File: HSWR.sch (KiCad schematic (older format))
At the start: 25 parts, among them J1 USB_B, J2 IO, J3 B+, J4 B-, J5 U, J6 V, J7 W

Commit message: - reworked IO section -> now fully isolated - added fan output - sensor IO is now differential - exposed differential UART interface - fan pin not defined yet!
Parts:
- removed J2: IO, Auktora:PinHeader_2x10_P2.54mm_Vertical, symbol HSWR:Conn_01x20_Male_56
- removed JP1: 5V/3V3, Jumper:SolderJumper-3_P1.3mm_Open_RoundedPad1.0x1.5mm, symbol Jumper:Jumper_3_Open
- removed JP2, JP3: opt., Jumper:SolderJumper-2_P1.3mm_Open_RoundedPad1.0x1.5mm, symbol Device:Jumper_NO_Small
- removed R1, R2: 1k, Resistor_SMD:R_0805_2012Metric, symbol Device:R
- removed R3, R4: 1k5, Resistor_SMD:R_0805_2012Metric, symbol Device:R
- added J2: IO, Connector_IDC:IDC-Header_2x08_P2.54mm_Vertical_Lock, symbol Connector:Conn_01x16_Male
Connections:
- net labels removed: +5V
- wire segments 87 -> 70

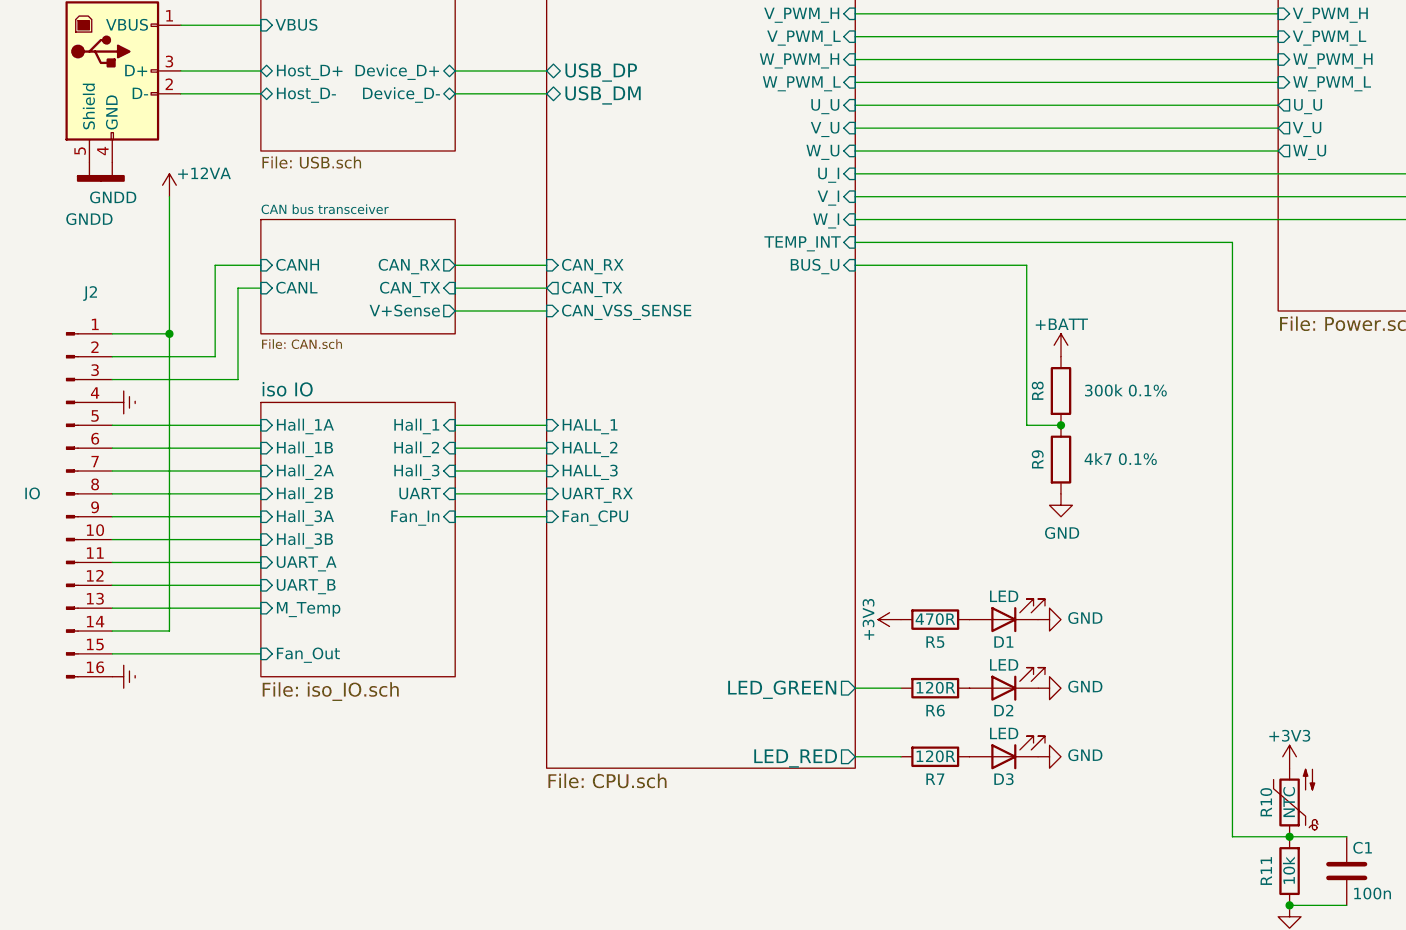
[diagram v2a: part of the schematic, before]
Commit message: - enlarged isolated island - bigger package for fan MOSFET - added 12V input protection - added U_DC sensing filter - added M_temp input filter - added reset pin decoupling for AVR - added HALL pull-ups - added TRI state selector jumper for buffer - removed UART selector jumper (AVR will check and switch to TRI state if needed)
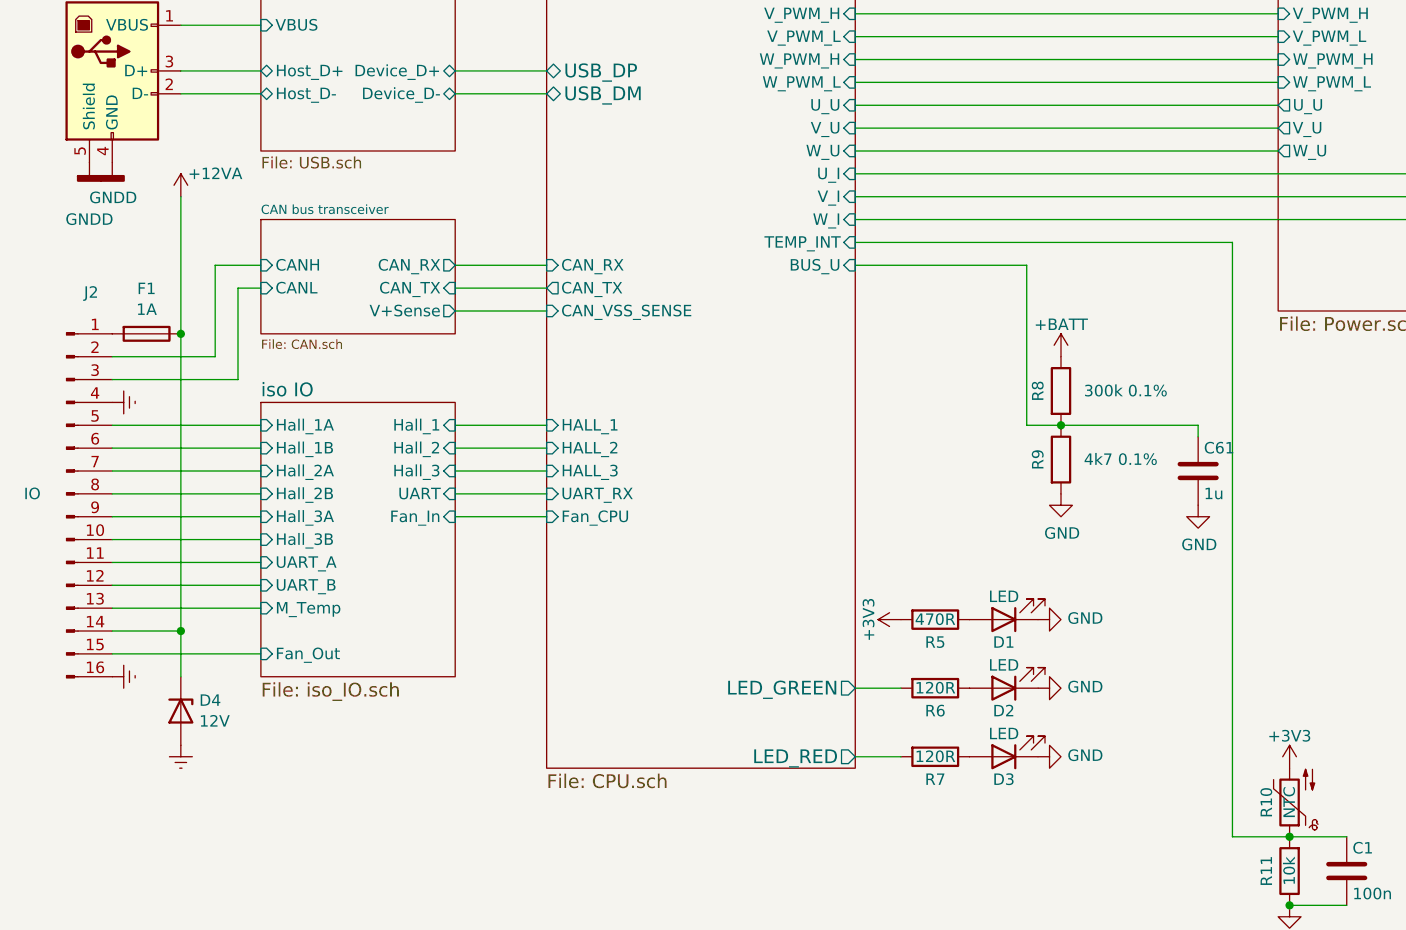
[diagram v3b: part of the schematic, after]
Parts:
- added C61: 1u, Capacitor_SMD:C_0805_2012Metric, symbol Device:C
- added D4: 12V, Diode_SMD:D_SMA, symbol Device:D_Zener
- added F1: 1A, Fuse:Fuse_Littelfuse-NANO2-451_453, symbol Device:Fuse
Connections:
- net +12VA: now also D4.1 (K), F1.1; no longer J2.1 (Pin_1)
- net Earth: now also D4.2 (A)
- net GND: now also C61.2
- net MCU/BUS_U: now also C61.1
- new net: F1.2, J2.1 (Pin_1)
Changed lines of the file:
@@
 EESchema Schematic File Version 4
+LIBS:HSWR-cache
 EELAYER 30 0
 EELAYER END
@@
 L power:+12VA #PWR03
 U 1 1 5C9EFA56
-P 1300 3500
-F 0 "#PWR03" H 1300 3350 50  0001 C CNN
-F 1 "+12VA" H 1450 3600 50  0000 C CNN
-F 2 "" H 1300 3500 50  0001 C CNN
-F 3 "" H 1300 3500 50  0001 C CNN
-	1    1300 3500
+P 1350 3500
+F 0 "#PWR03" H 1350 3350 50  0001 C CNN
+F 1 "+12VA" H 1500 3600 50  0000 C CNN
+F 2 "" H 1350 3500 50  0001 C CNN
+F 3 "" H 1350 3500 50  0001 C CNN
+	1    1350 3500
 	1    0    0    -1
 $EndComp
@@
 Connection ~ 6200 6600
 Wire Wire Line
-	1300 3500 1300 4100
-Wire Wire Line
-	1300 4100 1050 4100
-Wire Wire Line
 	1050 4200 1500 4200
 Wire Wire Line
@@
 	1700 5300 1050 5300
 Wire Wire Line
-	1300 4100 1300 5400
-Wire Wire Line
-	1300 5400 1050 5400
-Connection ~ 1300 4100
+	1350 5400 1050 5400
 $Comp
 L power:Earth #PWR0119
@@
 	1    0    0    -1
 $EndComp
+$Comp
+L Device:C C61
+U 1 1 5E6496A9
+P 5800 4700
+F 0 "C61" H 5825 4800 50  0000 L CNN
+F 1 "1u" H 5825 4600 50  0000 L CNN
+F 2 "Capacitor_SMD:C_0805_2012Metric" H 5838 4550 50  0001 C CNN
+F 3 "" H 5800 4700 50  0000 C CNN
+	1    5800 4700
+	1    0    0    -1
+$EndComp
+$Comp
+L power:GND #PWR0152
+U 1 1 5E64A18C
+P 5800 4850
+F 0 "#PWR0152" H 5800 4600 50  0001 C CNN
+F 1 "GND" H 5805 4677 50  0000 C CNN
+F 2 "" H 5800 4850 50  0001 C CNN
+F 3 "" H 5800 4850 50  0001 C CNN
+	1    5800 4850
+	1    0    0    -1
+$EndComp
+Wire Wire Line
+	5800 4550 5800 4500
+Wire Wire Line
+	5800 4500 5200 4500
+Wire Wire Line
+	1350 3500 1350 4100
+$Comp
+L Device:Fuse F1
+U 1 1 5E72429D
+P 1200 4100
+F 0 "F1" V 1003 4100 50  0000 C CNN
+F 1 "1A" V 1094 4100 50  0000 C CNN
+F 2 "Fuse:Fuse_Littelfuse-NANO2-451_453" V 1130 4100 50  0001 C CNN
+F 3 "~" H 1200 4100 50  0001 C CNN
+	1    1200 4100
+	0    1    1    0
+$EndComp
+Connection ~ 1350 4100
+Wire Wire Line
+	1350 4100 1350 5400
+$Comp
+L Device:D_Zener D4
+U 1 1 5E727A0D
+P 1350 5750
+F 0 "D4" V 1304 5830 50  0000 L CNN
+F 1 "12V" V 1395 5830 50  0000 L CNN
+F 2 "Diode_SMD:D_SMA" H 1350 5750 50  0001 C CNN
+F 3 "~" H 1350 5750 50  0001 C CNN
+	1    1350 5750
+	0    1    1    0
+$EndComp
+Wire Wire Line
+	1350 5400 1350 5600
+Connection ~ 1350 5400
+$Comp
+L power:Earth #PWR0155
+U 1 1 5E72D56C
+P 1350 5900
+F 0 "#PWR0155" H 1350 5650 50  0001 C CNN
+F 1 "Earth" H 1350 5750 50  0001 C CNN
+F 2 "" H 1350 5900 60  0000 C CNN
+F 3 "" H 1350 5900 60  0000 C CNN
+	1    1350 5900
+	1    0    0    -1
+$EndComp

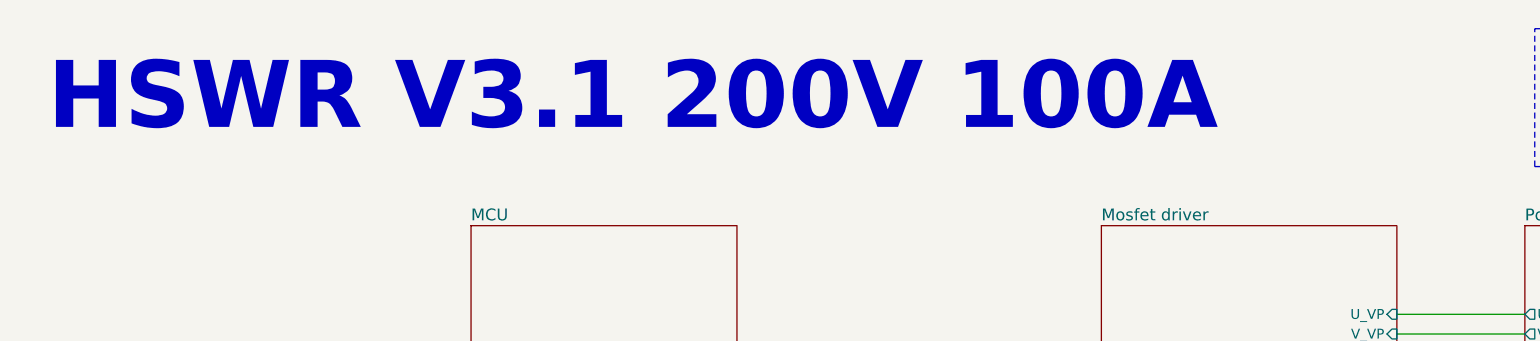
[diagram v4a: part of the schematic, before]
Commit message: - updated schematic textbox (version, author)
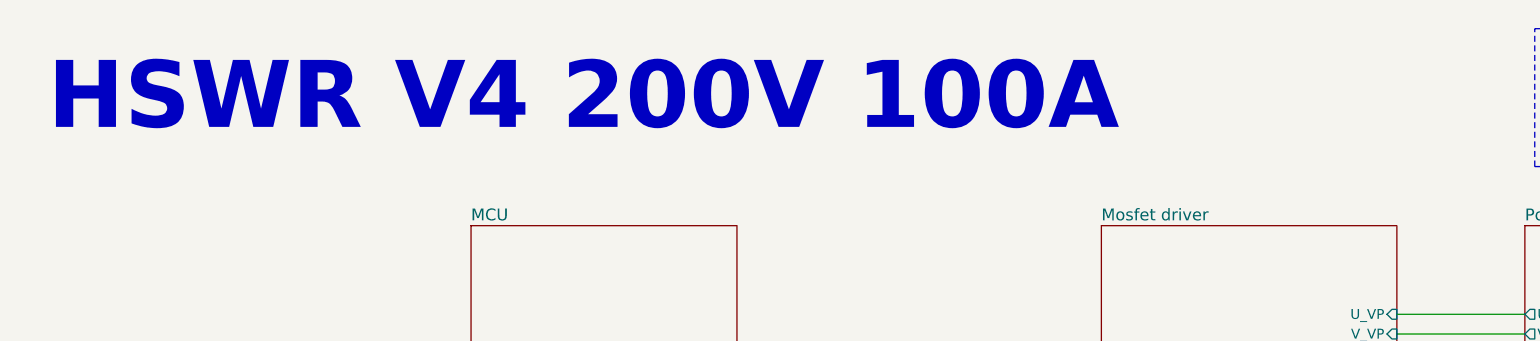
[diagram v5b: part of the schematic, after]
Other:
- note added: "HSWR V4 200V 100A"
- note removed: "HSWR V3.1 200V 100A"
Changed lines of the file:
@@
 Title "HSWR.0 200V 50A"
 Date "2017-02-05"
-Rev "2.0"
-Comp "Benjamin Vedder"
+Rev "4.0"
+Comp ""
 Comment1 ""
 Comment2 ""
 Comment3 ""
-Comment4 "Top level"
+Comment4 ""
 $EndDescr
 Text Notes 800  1200 0    340  ~ 68
-HSWR V3.1 200V 100A
+HSWR V4 200V 100A
 Wire Wire Line
 	7650 3900 8300 3900
